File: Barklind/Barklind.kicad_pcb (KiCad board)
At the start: 2 copper layers, 104 x 80.5 mm, 29 parts, among them J1 Molex 47053-1000, J2 Molex 47053-1000, J3 Molex 47053-1000, J4 RJ45_Abracon_ARJP11A-MASA-B-A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, J5 ESP_Socket[1..19], J6 ESP_Socket[20..38], U2 TPS2375-1, U3 W5500

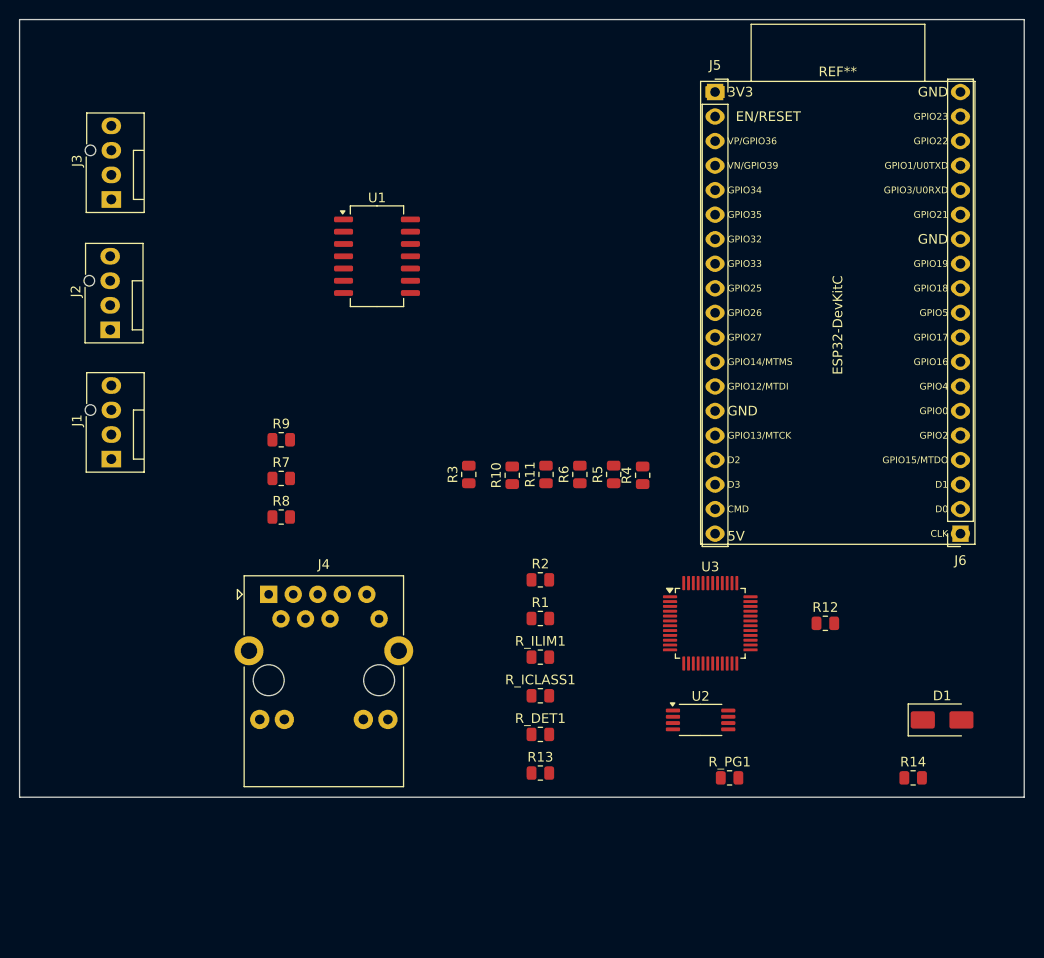
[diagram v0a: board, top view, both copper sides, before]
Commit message: Restructured project, Changed kibot configurations into different files Changed github actions for the different jobs
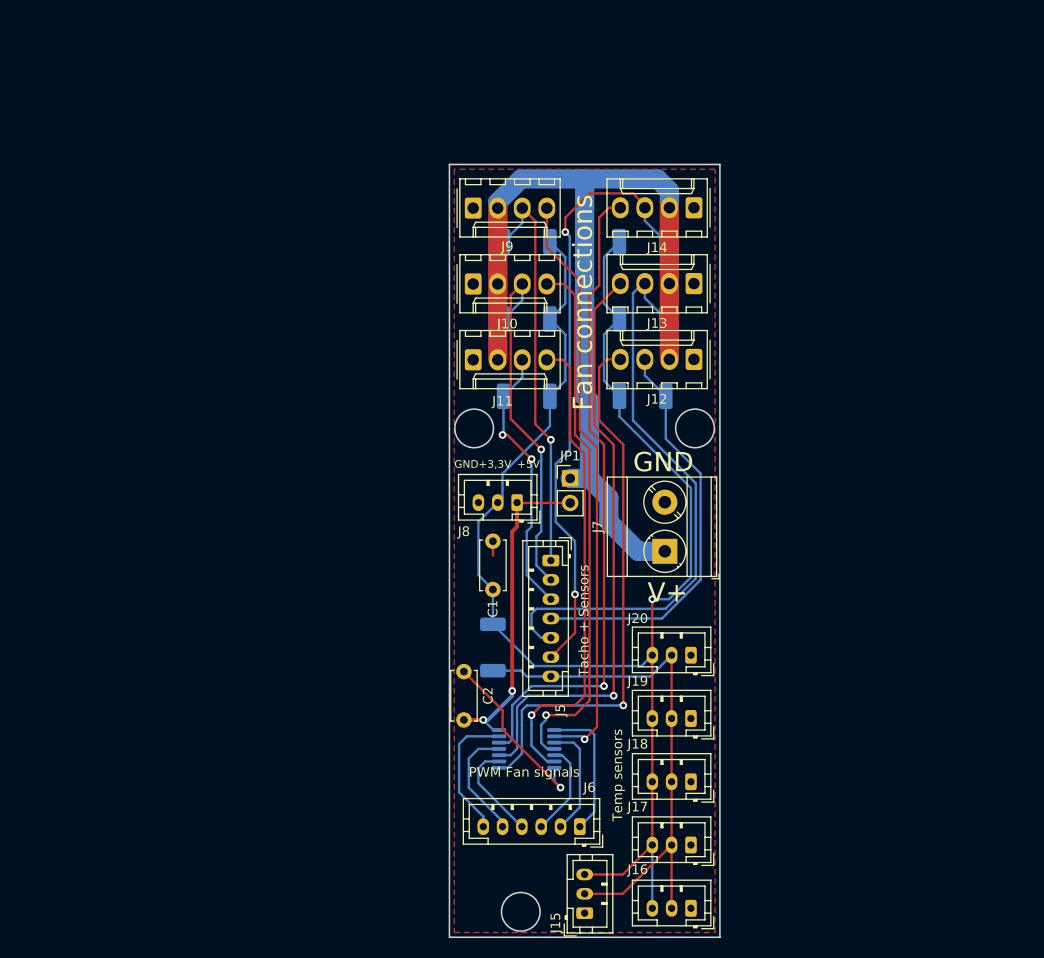
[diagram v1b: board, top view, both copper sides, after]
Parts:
- removed D1: SMAJ58A, Diode_SMD:D_SMA
- removed J1, J2, J3: Molex 47053-1000, Connector:FanPinHeader_1x04_P2.54mm_Vertical
- removed J4: RJ45_Abracon_ARJP11A-MASA-B-A-EMU2, Connector_RJ:RJ45_Abracon_ARJP11A-MA_Horizontal
- removed R10, R11, R8: 49R9, Resistor_SMD:R_0805_2012Metric
- removed R12: 0R, Resistor_SMD:R_0805_2012Metric
- removed R13: 1M, Resistor_SMD:R_0805_2012Metric
- removed R14: 12.4k, Resistor_SMD:R_0805_2012Metric
- removed R9: 10R, Resistor_SMD:R_0805_2012Metric
- removed REF**: ESP32-DevKitC, ESP32-Footprints:ESP32-DevKitC
- removed R_DET1, R_ICLASS1, R_ILIM1, R_PG1: TBD, Resistor_SMD:R_0805_2012Metric
- removed U1: ~, Package_SO:SO-14_5.3x10.2mm_P1.27mm
- removed U2: TPS2375-1, Package_SO:TSSOP-8_4.4x3mm_P0.65mm
- removed U3: W5500, Package_QFP:LQFP-48_7x7mm_P0.5mm
- added C1: 100 nF, Capacitor_THT:C_Disc_D5.0mm_W2.5mm_P5.00mm, F.Cu at (145.5, 83.5)
- added C2: 100 nF, Capacitor_THT:C_Disc_D5.0mm_W2.5mm_P5.00mm, F.Cu at (142.5, 97.0)
- added J10: Conn_01x04_Pin, Connector_Molex:Molex_KK-254_AE-6410-04A_1x04_P2.54mm_Vertical, F.Cu at (143.5, 56.9)
- added J11: Conn_01x04_Pin, Connector_Molex:Molex_KK-254_AE-6410-04A_1x04_P2.54mm_Vertical, F.Cu at (143.5, 64.7)
- added J12: Conn_01x04_Pin, Connector_Molex:Molex_KK-254_AE-6410-04A_1x04_P2.54mm_Vertical, F.Cu at (166.3, 64.7)
- added J13: Conn_01x04_Pin, Connector_Molex:Molex_KK-254_AE-6410-04A_1x04_P2.54mm_Vertical, F.Cu at (166.3, 56.8)
- added J14: Conn_01x04_Pin, Connector_Molex:Molex_KK-254_AE-6410-04A_1x04_P2.54mm_Vertical, F.Cu at (166.3, 49.0)
- added J15: Conn_01x03_Pin, Connector_JST:JST_PH_B3B-PH-K_1x03_P2.00mm_Vertical, F.Cu at (155.0, 122.0)
- added J16: Conn_01x03_Pin, Connector_JST:JST_PH_B3B-PH-K_1x03_P2.00mm_Vertical, F.Cu at (166.0, 121.5)
- added J17: Conn_01x03_Pin, Connector_JST:JST_PH_B3B-PH-K_1x03_P2.00mm_Vertical, F.Cu at (166.0, 115.0)
- added J18: Conn_01x03_Pin, Connector_JST:JST_PH_B3B-PH-K_1x03_P2.00mm_Vertical, F.Cu at (166.0, 108.4)
- added J19: Conn_01x03_Pin, Connector_JST:JST_PH_B3B-PH-K_1x03_P2.00mm_Vertical, F.Cu at (166.0, 101.8)
- added J20: Conn_01x03_Pin, Connector_JST:JST_PH_B3B-PH-K_1x03_P2.00mm_Vertical, F.Cu at (166.0, 95.3)
- added J7: Conn_01x02_Pin, TerminalBlock_Phoenix:TerminalBlock_Phoenix_MKDS-3-2-5.08_1x02_P5.08mm_Horizontal, F.Cu at (163.3, 84.5)
- added J8: Conn_01x03_Pin, Connector_JST:JST_PH_B3B-PH-K_1x03_P2.00mm_Vertical, F.Cu at (148.0, 79.5)
- added J9: Conn_01x04_Pin, Connector_Molex:Molex_KK-254_AE-6410-04A_1x04_P2.54mm_Vertical, F.Cu at (143.5, 49.0)
- added JP1: Jumper_2_Open, Connector_PinHeader_2.54mm:PinHeader_1x02_P2.54mm_Vertical, F.Cu at (153.5, 77.0)
- added U7: 74HCT04, Package_SO:TSSOP-14_4.4x5mm_P0.65mm, B.Cu at (149.0, 105.0)
- J5: value ESP_Socket[1..19] -> Conn_01x07_Pin; footprint Connector_PinSocket_2.54mm:PinSocket_1x19_P2.54mm_Vertical -> Connector_JST:JST_PH_B7B-PH-K_1x07_P2.00mm_Vertical
- J6: value ESP_Socket[20..38] -> Conn_01x06_Pin; footprint Connector_PinSocket_2.54mm:PinSocket_1x19_P2.54mm_Vertical -> Connector_JST:JST_PH_B6B-PH-K_1x06_P2.00mm_Vertical
- R1, R2, R3, R4: value 33R -> 10k; footprint Resistor_SMD:R_0805_2012Metric -> Resistor_SMD:R_2010_5025Metric_Pad1.40x2.65mm_HandSolder; moved to B.Cu
- R5, R6: value 330R -> 10k; footprint Resistor_SMD:R_0805_2012Metric -> Resistor_SMD:R_2010_5025Metric_Pad1.40x2.65mm_HandSolder; moved to B.Cu
- R7: value 49R9 -> 4,7k; footprint Resistor_SMD:R_0805_2012Metric -> Resistor_SMD:R_2010_5025Metric_Pad1.40x2.65mm_HandSolder; moved to B.Cu
- moved J5 51.4 mm to (151.5, 85.5), turned to -90 degrees
- moved J6 49.7 mm to (154.5, 113.0)
- moved R1 40.4 mm to (161.0, 52.5)
- moved R2 29.0 mm to (161.0, 60.5)
- moved R7 28.0 mm to (145.5, 94.5), turned to -90 degrees
- moved R6 24.7 mm to (149.0, 52.5), turned to 180 degrees
- moved R3 19.7 mm to (161.0, 68.5), turned to 0 degrees
- moved R5 18.4 mm to (149.0, 60.5), turned to 180 degrees
- moved R4 14.5 mm to (149.0, 68.5), turned to 180 degrees
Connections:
- J5 pad 1: /ESP_1 -> Net-(J5-Pin_1)
- J5 pad 2: /ESP_2 -> Net-(J10-Pin_3)
- J5 pad 3: /ESP_3 -> Net-(J11-Pin_3)
- J5 pad 4: /ESP_4 -> Net-(J12-Pin_3)
- J5 pad 5: /ESP_5 -> Net-(J13-Pin_3)
- J5 pad 6: /ESP_6 -> Net-(J14-Pin_3)
- J5 pad 7: /ESP_7 -> Net-(J15-Pin_2)
- J6 pad 1: /ESP_20 -> Net-(J6-Pin_1)
- J6 pad 2: /ESP_21 -> Net-(J6-Pin_2)
- J6 pad 3: /ESP_22 -> Net-(J6-Pin_3)
- J6 pad 4: /ESP_23 -> Net-(J6-Pin_4)
- J6 pad 5: /ESP_24 -> Net-(J6-Pin_5)
- J6 pad 6: /ESP_25 -> Net-(J6-Pin_6)
- R1 pad 1: Net-(U3-TXN) -> Net-(J15-Pin_3)
- R1 pad 2: /Ethernet/TD- -> Net-(J14-Pin_3)
- R2 pad 1: Net-(U3-TXP) -> Net-(J15-Pin_3)
- R2 pad 2: /Ethernet/TD+ -> Net-(J13-Pin_3)
- R3 pad 1: Net-(U3-RXN) -> Net-(J15-Pin_3)
- R3 pad 2: Net-(C11-Pad1) -> Net-(J12-Pin_3)
- R4 pad 1: Net-(U3-RXP) -> Net-(J15-Pin_3)
- R4 pad 2: Net-(C12-Pad1) -> Net-(J11-Pin_3)
- R5 pad 1: Net-(U3-LINKLED) -> Net-(J15-Pin_3)
- R5 pad 2: /Ethernet/LED_Y- -> Net-(J10-Pin_3)
- R6 pad 1: Net-(U3-ACTLED) -> Net-(J15-Pin_3)
- R6 pad 2: /Ethernet/LED_G- -> Net-(J5-Pin_1)
- R7 pad 1: +3.3VA -> Net-(J15-Pin_3)
- R7 pad 2: /Ethernet/TD+ -> Net-(J15-Pin_2)
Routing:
- net Net-(J15-Pin_3): track 0.00 -> 150.3 mm, vias 0 -> 1
- net /Signal conditioning/FanSupply: track 0.00 -> 98.6 mm
- net Net-(J14-Pin_4): track 0.00 -> 67.5 mm, vias 0 -> 1
- net Net-(J14-Pin_3): track 0.00 -> 62.6 mm, vias 0 -> 2
- net Net-(J13-Pin_4): track 0.00 -> 61.6 mm, vias 0 -> 1
- net Net-(J9-Pin_4): track 0.00 -> 60.9 mm, vias 0 -> 1
- net Net-(J13-Pin_3): track 0.00 -> 60.9 mm
- net Net-(J15-Pin_2): track 0.00 -> 57.0 mm
- net Net-(J12-Pin_4): track 0.00 -> 56.7 mm, vias 0 -> 1
- net Net-(J10-Pin_4): track 0.00 -> 55.8 mm, vias 0 -> 1
- net Net-(J11-Pin_4): track 0.00 -> 49.9 mm, vias 0 -> 1
- net Net-(J12-Pin_3): track 0.00 -> 42.4 mm
- net Net-(J5-Pin_1): track 0.00 -> 42.0 mm, vias 0 -> 1
- net Net-(J10-Pin_3): track 0.00 -> 37.7 mm, vias 0 -> 1
- net /Signal conditioning/Supply5V: track 0.00 -> 33.8 mm, vias 0 -> 2
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- added copper zone on F.Cu, net /Signal conditioning/GND
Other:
- board size 104 x 80.5 mm -> 28 x 80 mm
- board text added: "+3,3V"
- board text added: "+5V"
- board text added: "Barklind ESP32-POE Fan expansion V0.1"
- board text added: "Fan connections"
- board text added: "GND"
- board text added: "PWM Fan signals"
- board text added: "Tacho + Sensors"
- board text added: "Temp sensors"
- board text added: "V+"

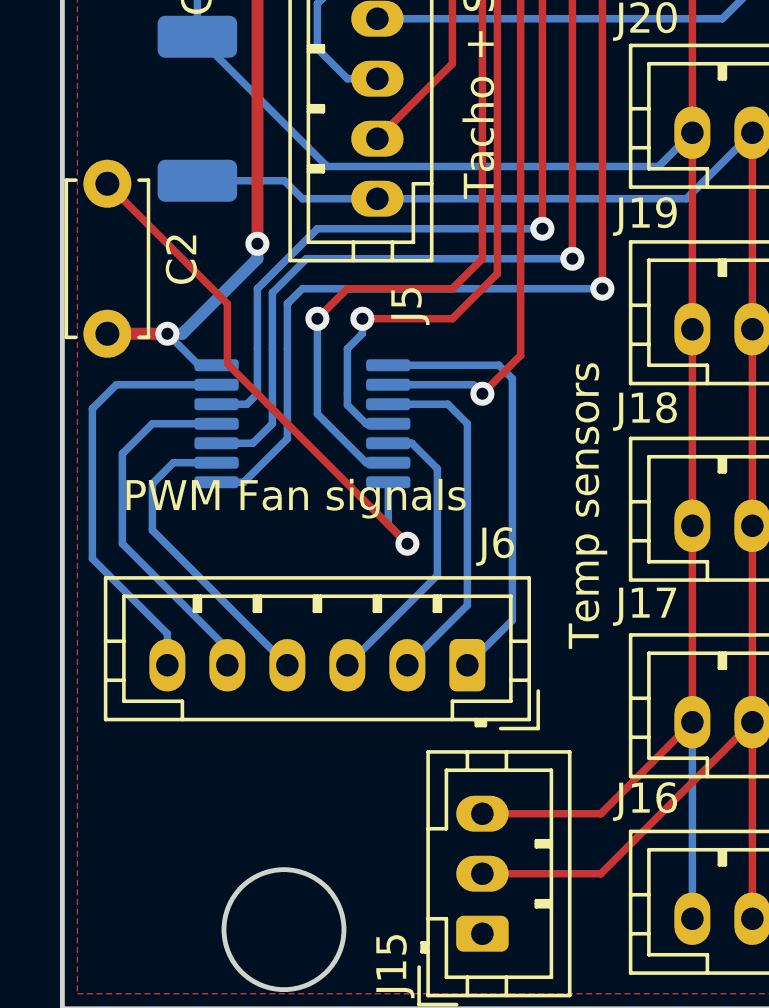
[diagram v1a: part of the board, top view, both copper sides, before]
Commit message: Added pin header for pulling down unused inverter inputs
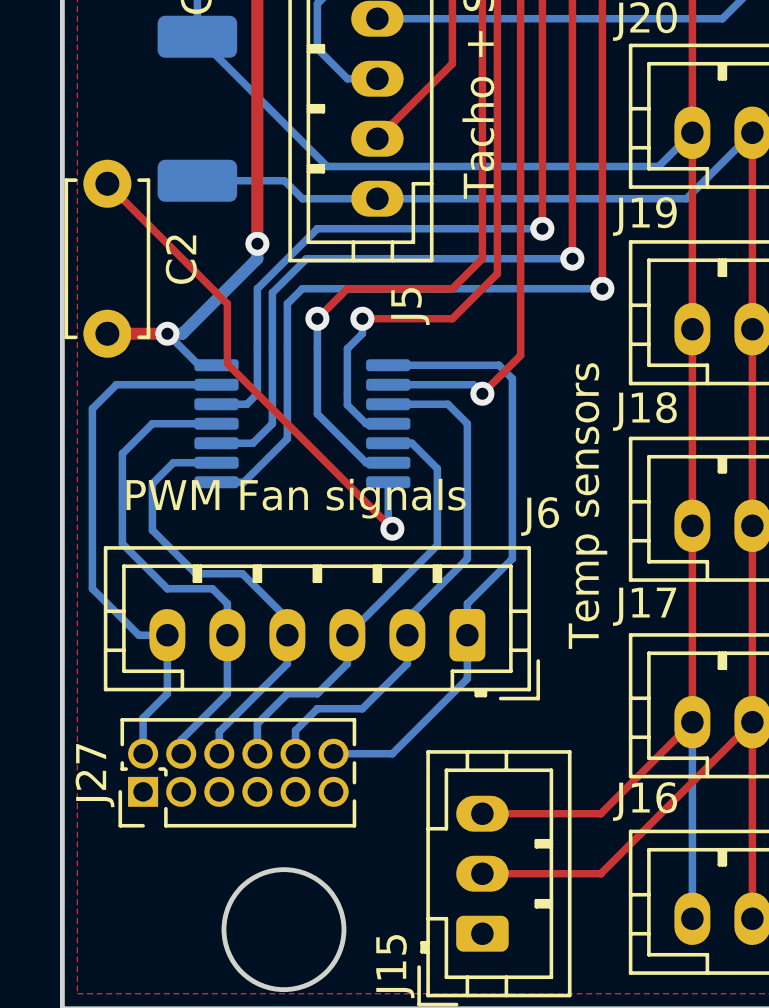
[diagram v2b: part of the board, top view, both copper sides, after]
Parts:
- added J27: Conn_02x06_Odd_Even, Connector_PinHeader_1.27mm:PinHeader_2x06_P1.27mm_Vertical, F.Cu at (143.7, 117.3)
- moved J6 1.00 mm to (154.5, 112.0)
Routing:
- net Net-(J27-Pin_12): track 14.5 -> 20.4 mm
- net Net-(J27-Pin_10): track 11.8 -> 17.2 mm
- net Net-(J27-Pin_6): track 10.3 -> 15.1 mm
- net Net-(J27-Pin_8): track 9.78 -> 14.6 mm
- net Net-(J27-Pin_4): track 12.1 -> 16.5 mm
- net Net-(J27-Pin_2): track 14.1 -> 17.9 mm
- net /Signal conditioning/GND: track 20.0 -> 18.5 mm

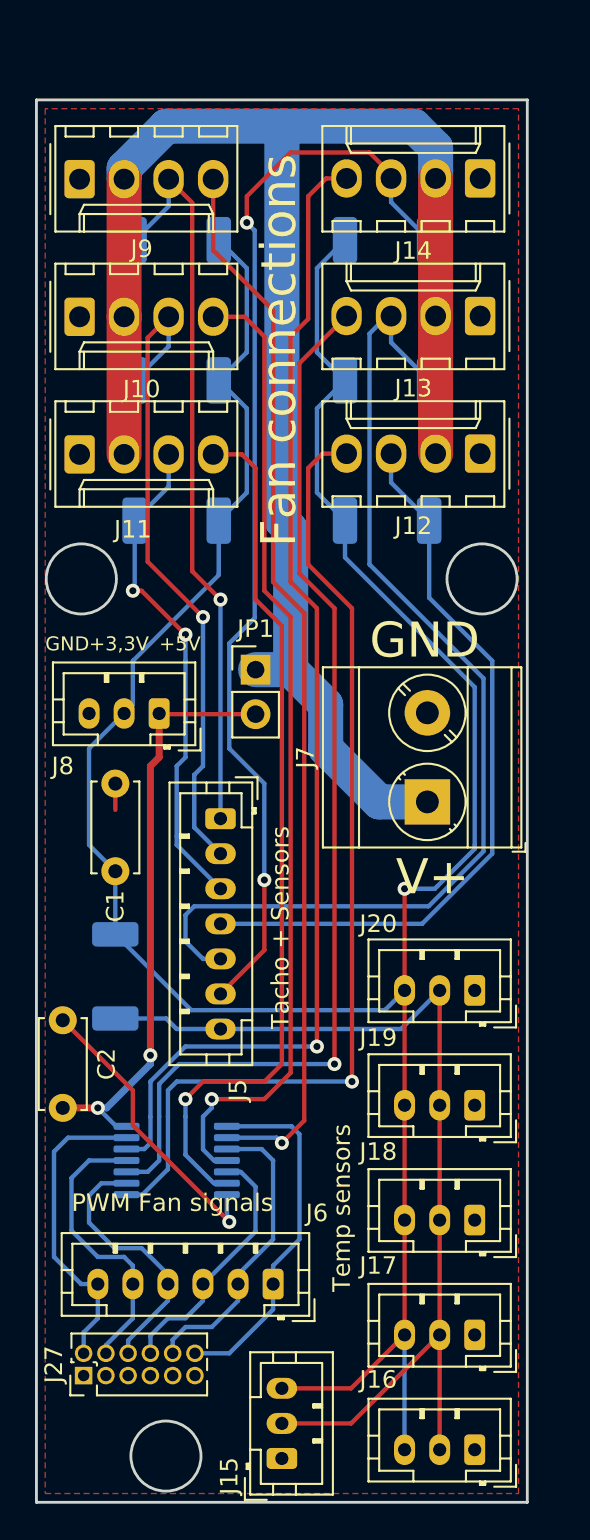
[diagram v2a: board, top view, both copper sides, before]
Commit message: Changed PCB to 4 layer and created manufacture files
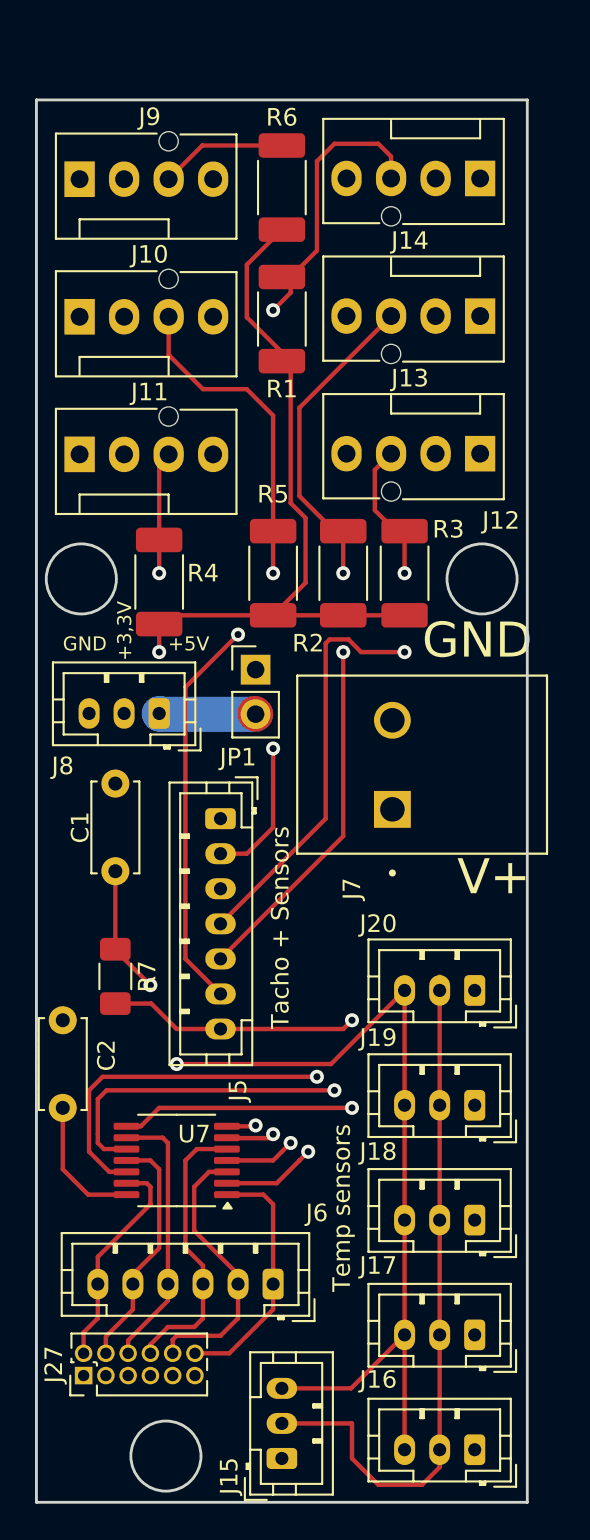
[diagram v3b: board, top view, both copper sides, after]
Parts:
- J10, J11, J12, J13, J14, J9: footprint Connector_Molex:Molex_KK-254_AE-6410-04A_1x04_P2.54mm_Vertical -> Connector:FanPinHeader_1x04_P2.54mm_Vertical
- J7: footprint TerminalBlock_Phoenix:TerminalBlock_Phoenix_MKDS-3-2-5.08_1x02_P5.08mm_Horizontal -> Phoenix:PHOENIX_1705469
- R1, R2, R3, R4, R5, R6, U7: moved to F.Cu
- R7: footprint Resistor_SMD:R_2010_5025Metric_Pad1.40x2.65mm_HandSolder -> Resistor_SMD:R_1206_3216Metric_Pad1.30x1.75mm_HandSolder; moved to F.Cu
- moved R5 12.3 mm to (154.5, 71.5), turned to 90 degrees
- moved R2 11.3 mm to (158.5, 71.5), turned to 90 degrees
- moved R1 7.50 mm to (155.0, 57.0), turned to 90 degrees
- moved J7 7.44 mm to (170.1, 87.5)
- moved R6 6.71 mm to (155.0, 49.5), turned to 90 degrees
- moved R4 3.64 mm to (148.0, 72.0), turned to 90 degrees
- moved R3 3.16 mm to (162.0, 71.5), turned to 90 degrees
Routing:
- net /Signal conditioning/FanSupply: track 98.6 -> 0.00 mm
- net Net-(J15-Pin_3): track 150.3 -> 116.8 mm, vias 1 -> 3
- net Net-(J13-Pin_3): track 60.9 -> 42.6 mm, vias 0 -> 2
- net /Signal conditioning/GND: track 18.5 -> 1.66 mm
- net Net-(J11-Pin_4): track 49.9 -> 42.9 mm
- net Net-(J12-Pin_3): track 42.4 -> 35.6 mm, vias 0 -> 2
- net Net-(J15-Pin_2): track 57.0 -> 63.6 mm, vias 0 -> 1
- net Net-(J27-Pin_12): track 20.4 -> 14.4 mm
- net /Signal conditioning/Supply5V: track 33.8 -> 39.6 mm, vias 2 -> 0
- net Net-(J27-Pin_2): track 17.9 -> 12.5 mm
- net Net-(J14-Pin_3): track 62.6 -> 57.6 mm
- net Net-(J14-Pin_4): track 67.5 -> 72.2 mm
- net Net-(J12-Pin_4): track 56.7 -> 52.1 mm
- net Net-(J5-Pin_1): track 42.0 -> 45.9 mm, vias 1 -> 0
- net Net-(J27-Pin_4): track 16.5 -> 13.8 mm
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- added copper zone on B.Cu, net /Signal conditioning/FanSupply
- added copper zone on In2.Cu, net /Signal conditioning/GND
- removed copper zone on F.Cu, net /Signal conditioning/GND
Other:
- copper layers 2 -> 4

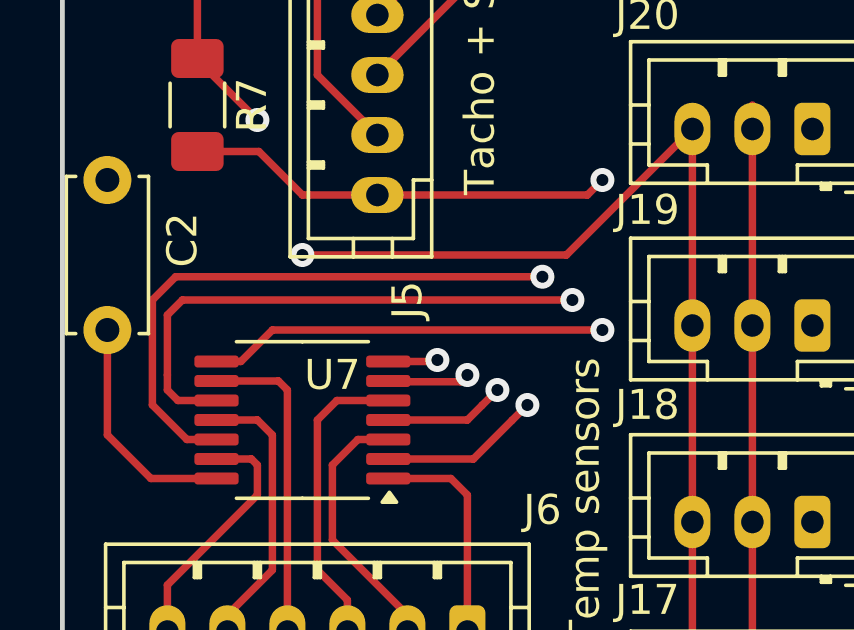
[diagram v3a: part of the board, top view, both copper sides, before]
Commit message: Separated signal GND and Power GND
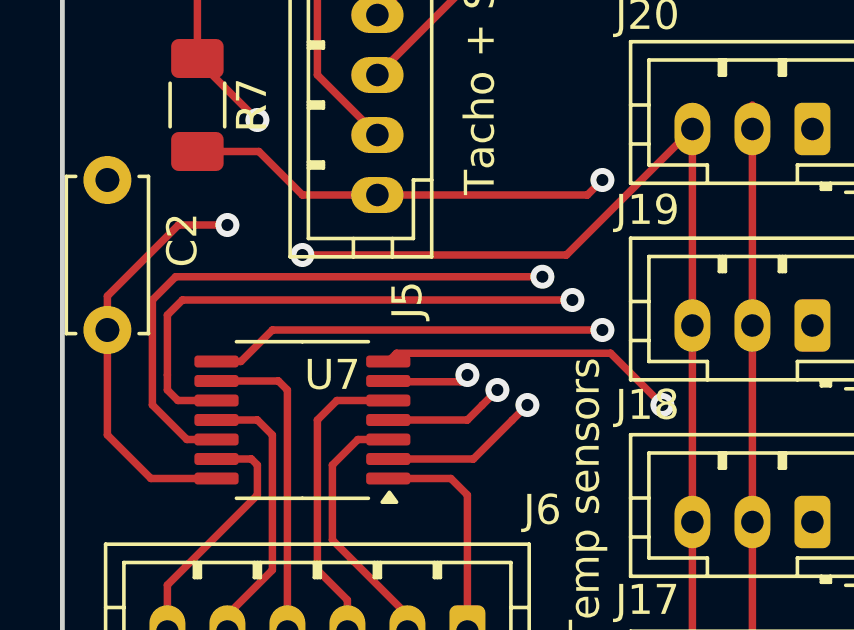
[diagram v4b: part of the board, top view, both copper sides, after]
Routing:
- net /Signal conditioning/GND: track 1.66 -> 95.9 mm
- net /Signal conditioning/Supply5V: track 39.6 -> 39.0 mm, vias 0 -> 1
